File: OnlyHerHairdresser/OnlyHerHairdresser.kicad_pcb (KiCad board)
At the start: 8 copper layers, 179 x 47 mm, 4 parts

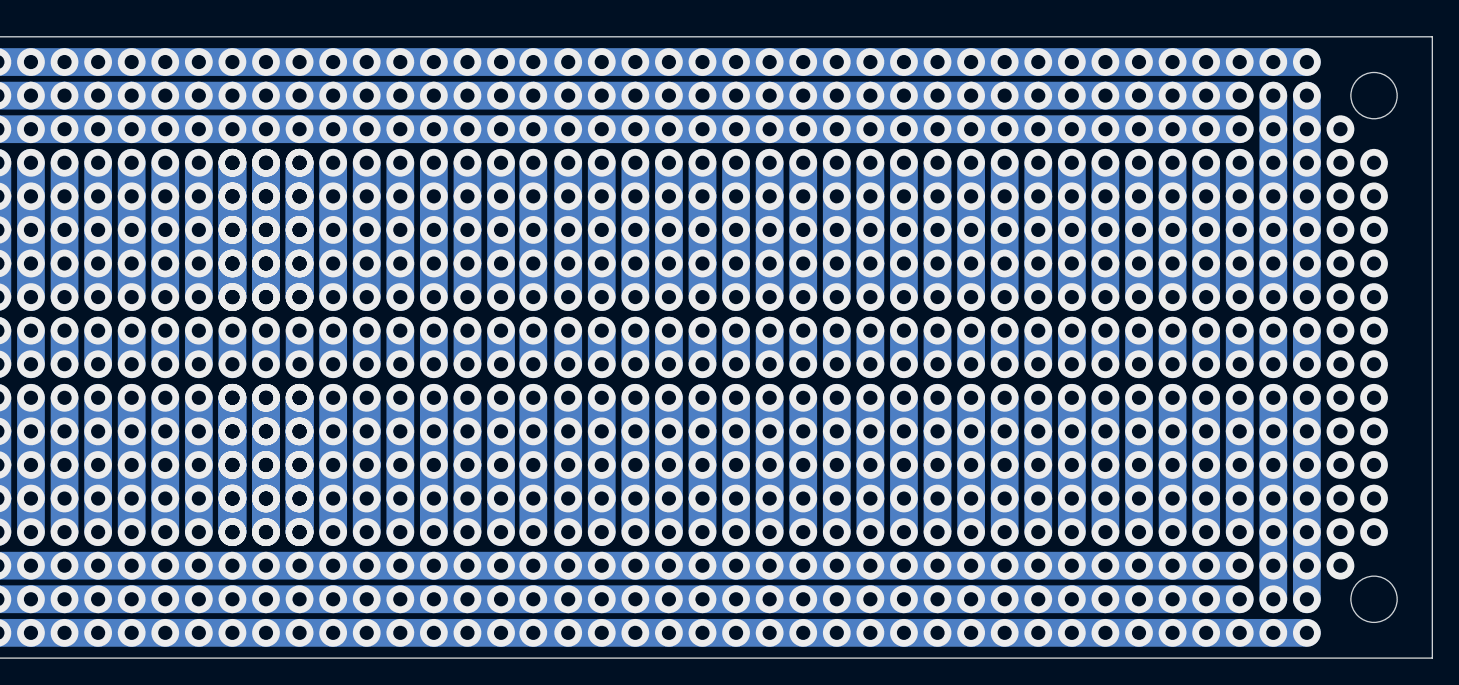
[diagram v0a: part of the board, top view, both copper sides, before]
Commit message: OnlyHerHairdresser: circuit designed and board laid out
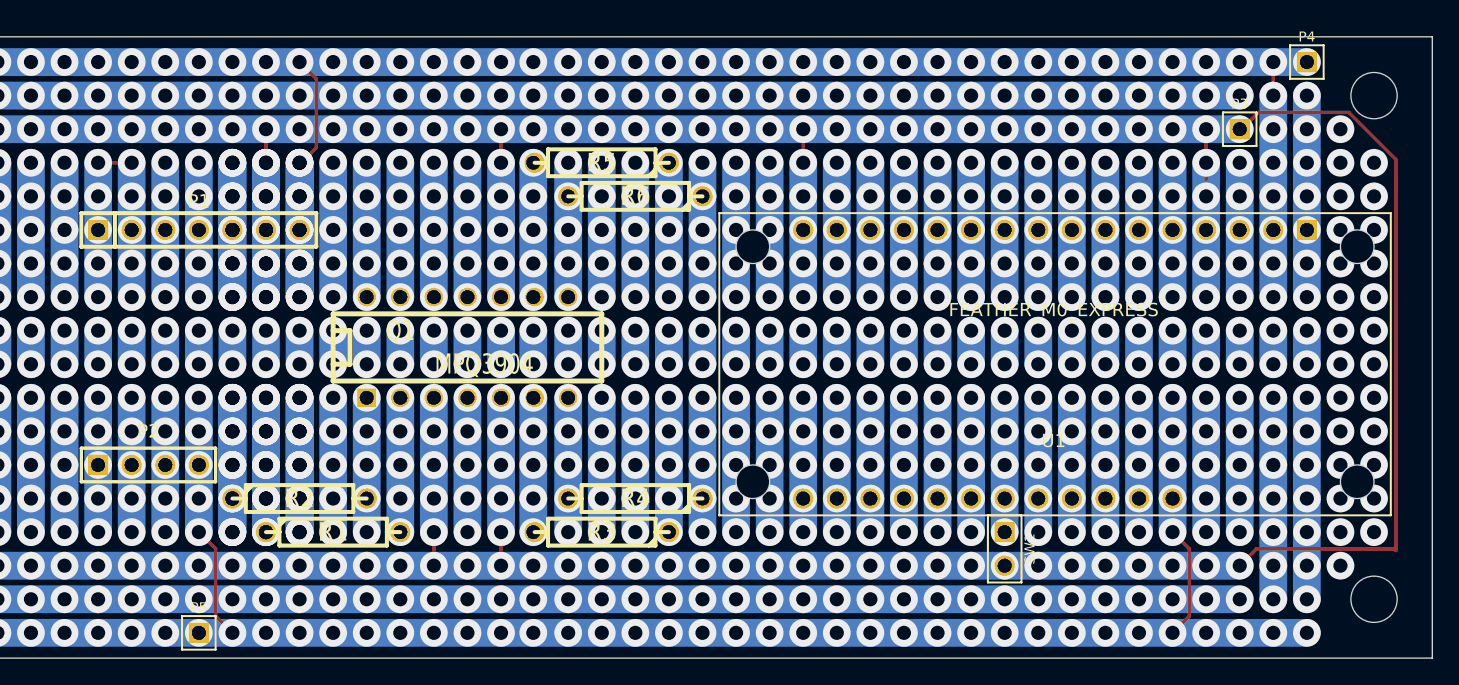
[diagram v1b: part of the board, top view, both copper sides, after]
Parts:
- added P1: TCS34725 Breakout, PIN_ARRAY-7X1, F.Cu at (116.8, 68.6)
- added P2: RGB LEDS, PIN_ARRAY_4x1, F.Cu at (113.0, 86.4)
- added P3: CONN_1, PIN_ARRAY_1, F.Cu at (195.6, 61.0)
- added P4: CONN_1, PIN_ARRAY_1, F.Cu at (200.7, 55.9)
- added P5: CONN_1, PIN_ARRAY_1, F.Cu at (116.8, 99.1)
- added Q1: MPQ3904, DIP-14__300, F.Cu at (137.2, 77.5)
- added R1: 1K Ohms, R4, F.Cu at (127.0, 91.4)
- added R2: 45 Ohms, R4, F.Cu at (124.5, 88.9)
- added R3: 1K Ohms, R4, F.Cu at (147.3, 91.4)
- added R4: 45 Ohms, R4, F.Cu at (149.9, 88.9)
- added R5: 1K Ohms, R4, F.Cu at (147.3, 63.5)
- added R6: 45 Ohms, R4, F.Cu at (149.9, 66.0)
- added SW1: SW_PUSH, PIN_ARRAY_2X1, F.Cu at (177.8, 92.7)
- added U1: FEATHER_M0_EXPRESS, AdafruitFeather, F.Cu at (181.6, 78.7)
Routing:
- net (no net): track 2486.7 -> 1465.6 mm, vias 1236 -> 791
- net /GND: track 0.00 -> 443.1 mm, vias 0 -> 155
- net /VIN: track 0.00 -> 206.9 mm, vias 0 -> 81
- net /Comm: track 0.00 -> 197.7 mm, vias 0 -> 74
- net /SDA: track 0.00 -> 87.4 mm, vias 0 -> 10
- net /SCL: track 0.00 -> 87.4 mm, vias 0 -> 10
- net N-0000013: track 0.00 -> 84.9 mm, vias 0 -> 15
- net /B: track 0.00 -> 67.0 mm, vias 0 -> 10
- net /G: track 0.00 -> 64.6 mm, vias 0 -> 10
- net N-0000010: track 0.00 -> 54.4 mm, vias 0 -> 10
- net /R: track 0.00 -> 41.7 mm, vias 0 -> 15
- net N-0000012: track 0.00 -> 39.2 mm, vias 0 -> 10
- net /INT: track 0.00 -> 22.9 mm, vias 0 -> 10
- net N-000009: track 0.00 -> 10.2 mm, vias 0 -> 5
- net N-000008: track 0.00 -> 10.2 mm, vias 0 -> 5
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
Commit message: Add Life2.
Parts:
- removed ? (x4): , MH
- removed P3, P4, P5: CONN_1, PIN_ARRAY_1
- moved R5 76.2 mm to (133.3, 138.4), turned to 0 degrees
- moved R6 72.4 mm to (130.8, 135.9), turned to 0 degrees
- moved P1 70.0 mm to (113.0, 138.4)
- moved U1 51.6 mm to (190.5, 129.5), turned to 0 degrees
- moved Q1 51.2 mm to (143.5, 128.3), turned to 180 degrees
- moved R2 44.9 mm to (156.2, 120.7), turned to 180 degrees
- moved R1 37.7 mm to (153.7, 118.1), turned to 180 degrees
- moved R4 37.0 mm to (130.8, 120.7), turned to 0 degrees
- moved P2 32.0 mm to (116.8, 118.1)
- moved R3 30.1 mm to (133.3, 118.1), turned to 0 degrees
- moved SW1 23.3 mm to (194.3, 109.2), turned to 90 degrees
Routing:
- net (no net): track 1465.6 -> 0.00 mm, vias 791 -> 0
- net /VIN: track 206.9 -> 69.8 mm, vias 81 -> 0
- net /GND: track 443.1 -> 308.6 mm, vias 155 -> 0
- net /Comm: track 197.7 -> 80.0 mm, vias 74 -> 0
- net /SDA: track 87.4 -> 166.4 mm, vias 10 -> 0
- net N-0000010: track 54.4 -> 118.1 mm, vias 10 -> 0
- net /G: track 64.6 -> 12.7 mm, vias 10 -> 0
- net N-0000012: track 39.2 -> 87.6 mm, vias 10 -> 0
- net /B: track 67.0 -> 25.4 mm, vias 10 -> 0
- net N-0000013: track 84.9 -> 49.5 mm, vias 15 -> 0
- net /SCL: track 87.4 -> 120.7 mm, vias 10 -> 0
- net /R: track 41.7 -> 66.0 mm, vias 15 -> 0
- net /INT: track 22.9 -> 2.54 mm, vias 10 -> 0
- net N-000006: track 10.2 -> 3.81 mm, vias 5 -> 0
- net N-000004: track 10.2 -> 3.81 mm, vias 5 -> 0
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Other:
- board outline removed
- copper layers 8 -> 6
